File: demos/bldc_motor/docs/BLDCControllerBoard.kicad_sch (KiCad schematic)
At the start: 10 parts, among them J1 Header1xNFemale, J2 Header1xNFemale, J3 Header1xNFemale

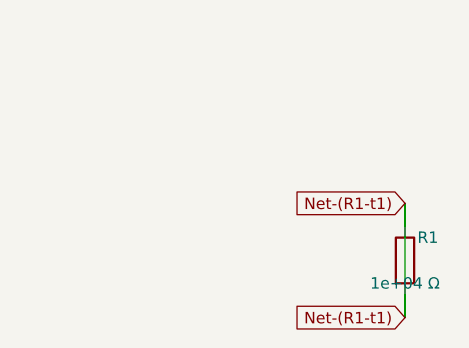
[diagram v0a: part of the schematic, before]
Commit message: units: Ohms.__str__ uses engineering notation (kΩ, MΩ, GΩ)
The previous `Ohms.__str__` formatted with bare `:.3g`, producing
unreadable scientific output for clean kilo / mega multiples:

  str(Ohms(10_000))     == "1e+04 Ω"      → now "10 kΩ"
  str(Ohms(100_000))    == "1e+05 Ω"      → now "100 kΩ"
  str(Ohms(1_000_000))  == "1e+06 Ω"      → now "1 MΩ"

The breadboard SVG visualiser surfaced the problem: a resistor body
labelled "100000Ω" makes a reader count zeros, while a label of
"100 kΩ" reads at a glance — exactly the convention every schematic
and parts catalogue uses. Centralising the engineering notation in
`Ohms.__str__` means every downstream consumer (assembly guide,
breadboard SVG, kicad netlist, BOM, reports) inherits the readable
form without each format adapter rolling its own formatter.

  - `Ohms.__str__` returns "47 Ω", "4.7 kΩ", "10 kΩ", "100 kΩ",
    "1 MΩ", "10 MΩ", "1 GΩ" per the kilo / mega / giga thresholds.
  - `Resistor.__str__` delegates to `str(self._ohms)` so it
    inherits the new notation (was producing the noisy "47.0 Ω"
    via raw float).
  - The breadboard visualiser's resistor body label uses
    `str(part.ohms)` directly (previously had a private
    `_format_ohms_compact` helper; removed).
  - `tests/components/test_resistor.py::test_str` updated for
    "47 Ω" (was "47.0 Ω"); new `test_str_renders_in_engineering_notation`
    pins kΩ / MΩ output across the kilo and mega thresholds.
  - All demo docs / goldens refreshed where the Ohms.__str__
    change affected the rendered output (breadboard SVGs, kicad
    sch value fields, BOM rows).
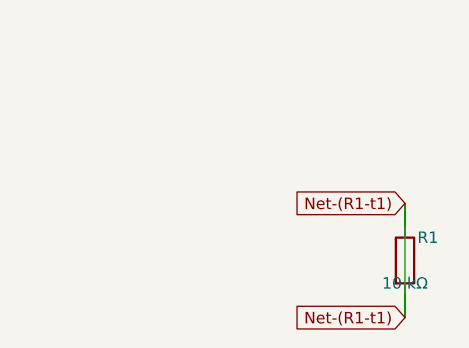
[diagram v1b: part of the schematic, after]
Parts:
- R1: value 1e+04 Ω -> 10 kΩ
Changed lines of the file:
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@@
       (effects (font (size 1.27 1.27)))
     )
-    (property "Value" "1e+04 Ω"
+    (property "Value" "10 kΩ"
       (at 63.5 561.34 0)
       (effects (font (size 1.27 1.27)))

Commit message: units: Farads + Henries __str__ also use engineering notation
Same treatment as `Ohms.__str__` (previous commit) for the other two
passive engineering quantities. Demos contain caps and inductors
with values that the bare `:.3g` formatter would emit in scientific
form (`1e-07 F` for a 100 nF decoupling cap); centralising the
engineering notation on the unit class means every consumer
(reports, BOM, breadboard SVG, etc.) inherits the readable form.

  - `Farads.__str__` returns `100 pF`, `22 nF`, `100 nF`, `1 µF`,
    `4.7 µF`, `470 µF`, `1 mF`, `1 F` across the standard
    capacitance bands.
  - `Henries.__str__` returns `100 nH`, `10 µH`, `22 mH`, `1 H`
    across the standard inductance bands.
  - `Capacitor.__str__` and `Inductor.__str__` delegate to the
    unit class's str (were rolling raw-float formatters).
  - `framework.export.reports_common.part_description` now uses
    `str(part.ohms / farads / henries)` directly instead of the
    parallel `_format_ohms` / `_format_farads` / `_format_henries`
    helpers (removed — they duplicated the new logic on raw
    floats).
  - Breadboard SVG renderer now also labels capacitor and inductor
    bodies with their engineering-notation value (was only
    resistors).
  - `tests/framework/test_units.py`: parametrised regression tests
    for both unit classes across every band.
  - All affected demo docs / goldens refreshed.
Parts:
- C1, C2, C3, C4: value 1e-08 F -> 10 nF
- C5: value 1e-07 F -> 100 nF
- C6: value 1e-05 F -> 10 µF
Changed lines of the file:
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@@
       (effects (font (size 1.27 1.27)))
     )
-    (property "Value" "1e-08 F"
+    (property "Value" "10 nF"
       (at 63.5 27.94 0)
       (effects (font (size 1.27 1.27)))
@@
       (effects (font (size 1.27 1.27)))
     )
-    (property "Value" "1e-08 F"
+    (property "Value" "10 nF"
       (at 63.5 66.04 0)
       (effects (font (size 1.27 1.27)))
@@
       (effects (font (size 1.27 1.27)))
     )
-    (property "Value" "1e-08 F"
+    (property "Value" "10 nF"
       (at 63.5 104.14 0)
       (effects (font (size 1.27 1.27)))
@@
       (effects (font (size 1.27 1.27)))
     )
-    (property "Value" "1e-08 F"
+    (property "Value" "10 nF"
       (at 63.5 142.24 0)
       (effects (font (size 1.27 1.27)))
@@
       (effects (font (size 1.27 1.27)))
     )
-    (property "Value" "1e-07 F"
+    (property "Value" "100 nF"
       (at 63.5 180.34 0)
       (effects (font (size 1.27 1.27)))
@@
       (effects (font (size 1.27 1.27)))
     )
-    (property "Value" "1e-05 F"
+    (property "Value" "10 µF"
       (at 63.5 218.44 0)
       (effects (font (size 1.27 1.27)))
